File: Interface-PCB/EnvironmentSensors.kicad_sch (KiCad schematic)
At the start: 30 parts, among them IC1 SN74LVC245AN, J10 LEVEL_SENSOR, J11 TEMPERATURE_SENSOR, J12 TEMPERATURE_SENSOR, J5 LEVEL_SENSOR, J6 LEVEL_SENSOR, J7 LEVEL_SENSOR, J8 LEVEL_SENSOR, J9 LEVEL_SENSOR

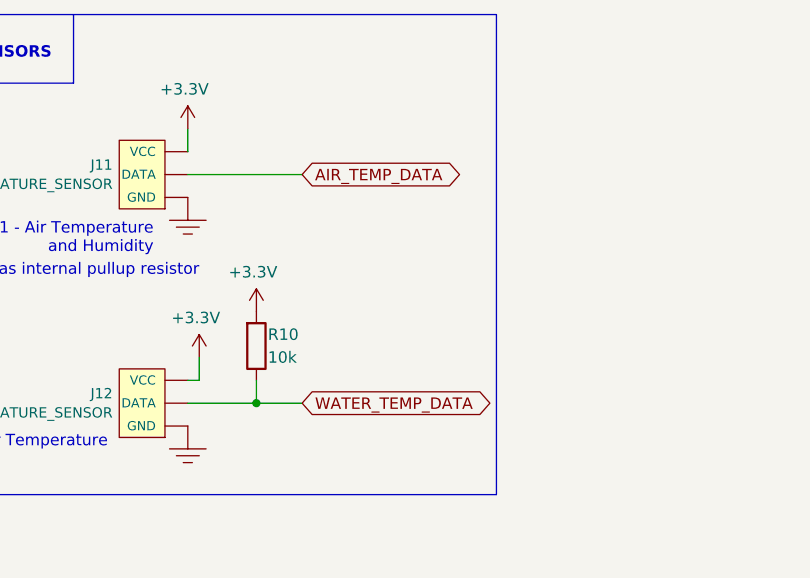
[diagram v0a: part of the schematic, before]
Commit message: Complete PCB layout
- Complete component positioning and PCB layout
- Swap most pin assignments to resolve track route criss-crossing
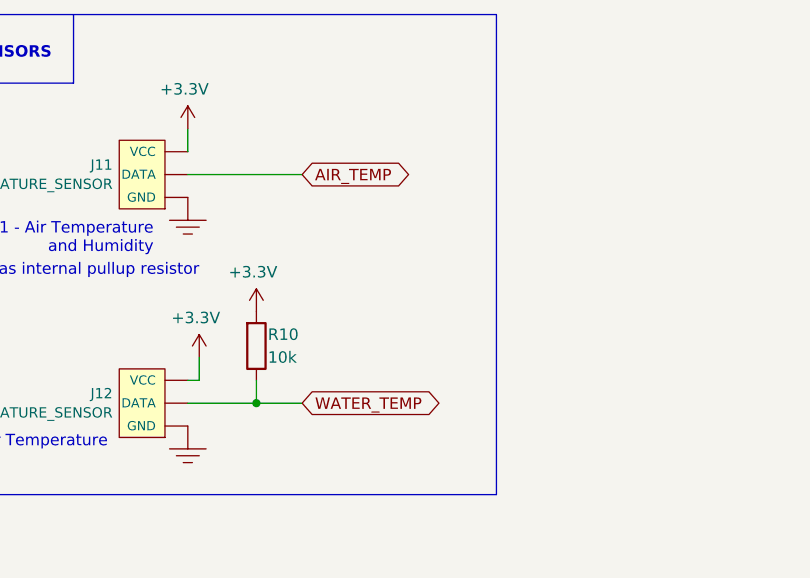
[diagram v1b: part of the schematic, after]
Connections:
- net AIR_TEMP_DATA renamed AIR_TEMP
- net WATER_TEMP_DATA renamed WATER_TEMP
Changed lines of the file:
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@@
     (effects (font (size 1.27 1.27)) (justify left bottom))
   )
-  (global_label "WATER_TEMP_DATA" (shape bidirectional) (at 166.37 119.38 0) (fields_autoplaced)
+  (global_label "WATER_TEMP" (shape bidirectional) (at 166.37 119.38 0) (fields_autoplaced)
     (effects (font (size 1.27 1.27)) (justify left))
-    (property "Intersheet References" "${INTERSHEET_REFS}" (id 0) (at -95.25 -33.02 0)
-      (effects (font (size 1.27 1.27)) hide)
+    (property "Intersheet References" "${INTERSHEET_REFS}" (id 0) (at 180.4266 119.3006 0)
+      (effects (font (size 1.27 1.27)) (justify left) hide)
     )
   )
@@
     )
   )
-  (global_label "AIR_TEMP_DATA" (shape bidirectional) (at 166.37 93.98 0) (fields_autoplaced)
+  (global_label "AIR_TEMP" (shape bidirectional) (at 166.37 93.98 0) (fields_autoplaced)
     (effects (font (size 1.27 1.27)) (justify left))
-    (property "Intersheet References" "${INTERSHEET_REFS}" (id 0) (at -92.71 -31.75 0)
-      (effects (font (size 1.27 1.27)) hide)
+    (property "Intersheet References" "${INTERSHEET_REFS}" (id 0) (at 177.4632 93.9006 0)
+      (effects (font (size 1.27 1.27)) (justify left) hide)
     )
   )

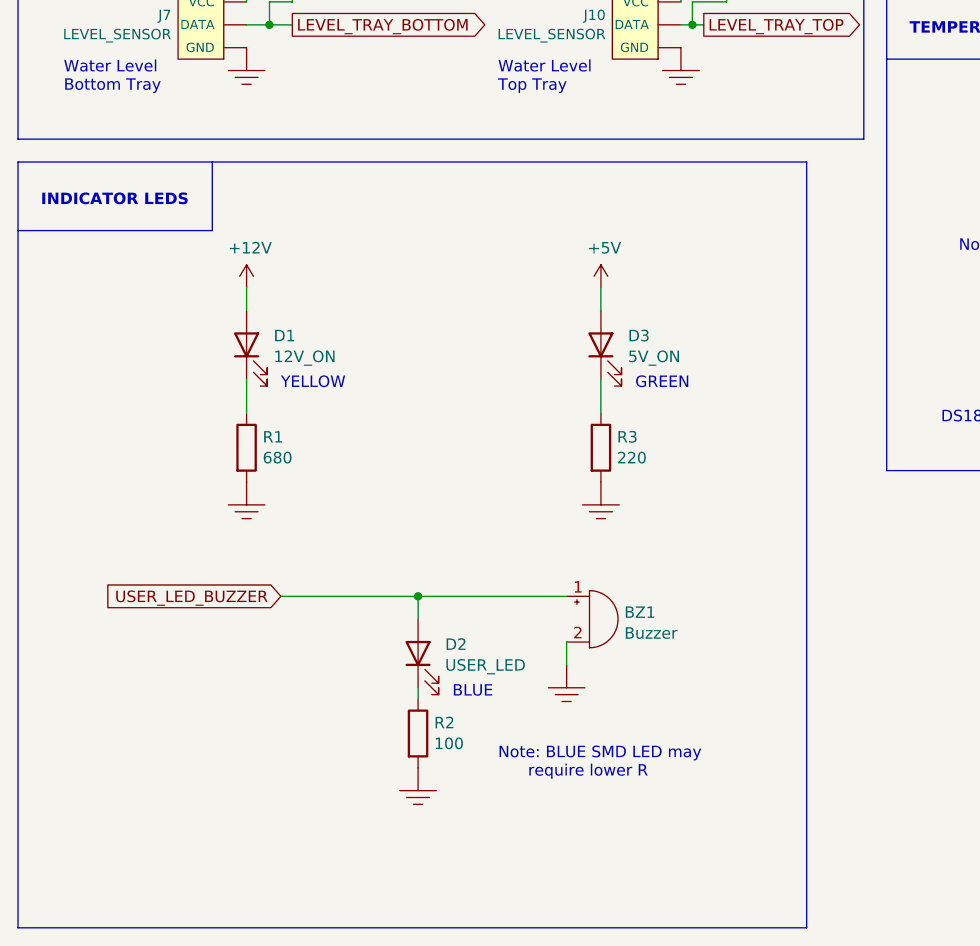
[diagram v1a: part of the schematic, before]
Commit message: Update Blue LED resistor value
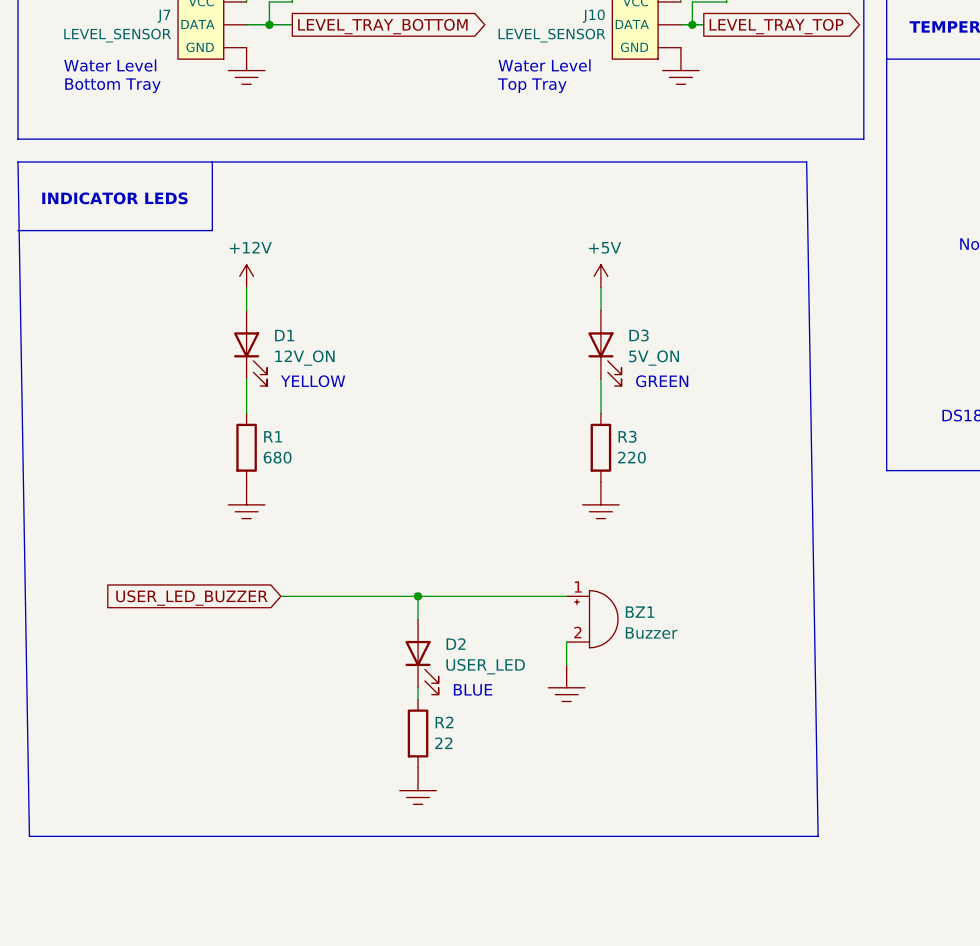
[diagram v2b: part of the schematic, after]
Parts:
- R2: value 100 -> 22
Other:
- note removed: "Note: BLUE SMD LED may require lower R"
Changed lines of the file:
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@@
     (stroke (width 0) (type default) (color 0 0 0 0))
   )
-  (polyline (pts (xy 102.87 180.34) (xy 102.87 95.25))
+  (polyline (pts (xy 104.14 170.18) (xy 102.87 95.25))
     (stroke (width 0) (type default) (color 0 0 0 0))
   )
@@
     (stroke (width 0) (type default) (color 0 0 0 0))
   )
-  (polyline (pts (xy 15.24 180.34) (xy 102.87 180.34))
+  (polyline (pts (xy 16.51 170.18) (xy 104.14 170.18))
     (stroke (width 0) (type default) (color 0 0 0 0))
   )
@@
     (stroke (width 0) (type default) (color 0 0 0 0))
   )
-  (polyline (pts (xy 15.24 95.25) (xy 15.24 180.34))
+  (polyline (pts (xy 15.24 95.25) (xy 16.51 170.18))
     (stroke (width 0) (type default) (color 0 0 0 0))
   )
@@
   (text "Note: Sensor has internal pullup resistor" (at 154.94 105.41 180)
     (effects (font (size 1.27 1.27)) (justify right bottom))
-  )
-  (text "Note: BLUE SMD LED may \n      require lower R" (at 68.58 163.83 0)
-    (effects (font (size 1.27 1.27)) (justify left bottom))
   )
   (text "Current limiting resistors, to avoid signal ringing"
@@
       (effects (font (size 1.27 1.27)) (justify left))
     )
-    (property "Value" "100" (id 1) (at 61.468 159.893 0)
-      (effects (font (size 1.27 1.27)) (justify left))
-    )
+    (property "Value" "22" (id 1) (at 61.468 159.893 0)
+      (effects (font (size 1.27 1.27)) (justify left))
+    )
